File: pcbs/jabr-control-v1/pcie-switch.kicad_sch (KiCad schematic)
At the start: 54 parts, among them U303 PI7C9X2G304SL

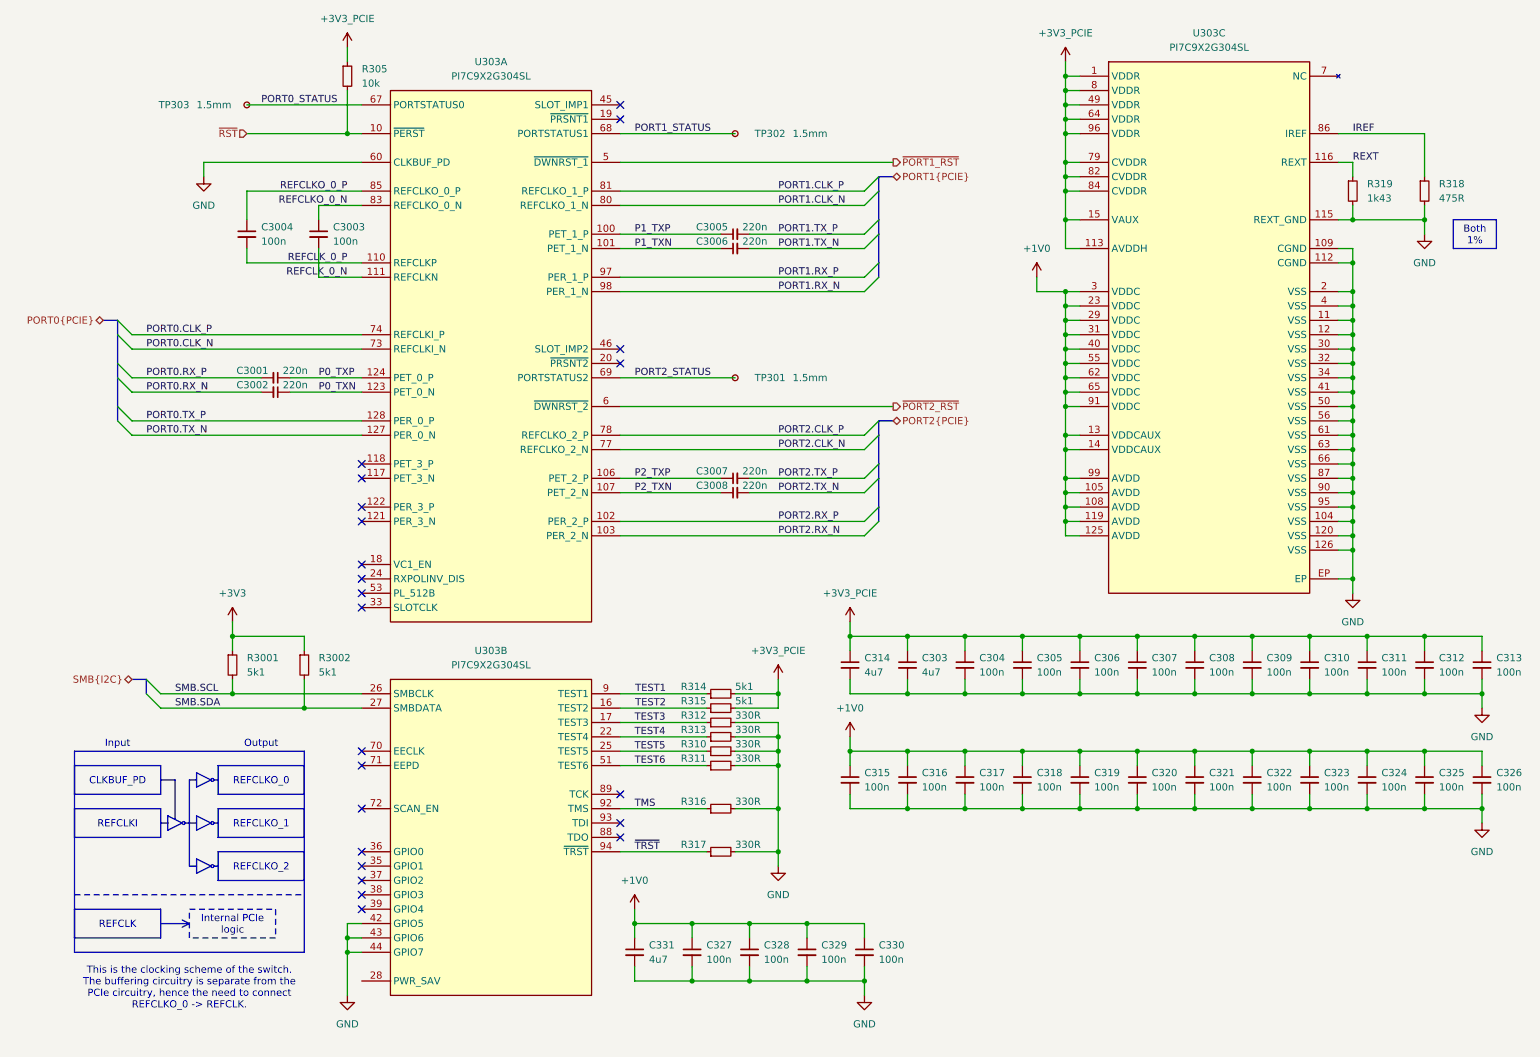
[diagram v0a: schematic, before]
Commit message: Updated FH12-22S-0.5SH footprints
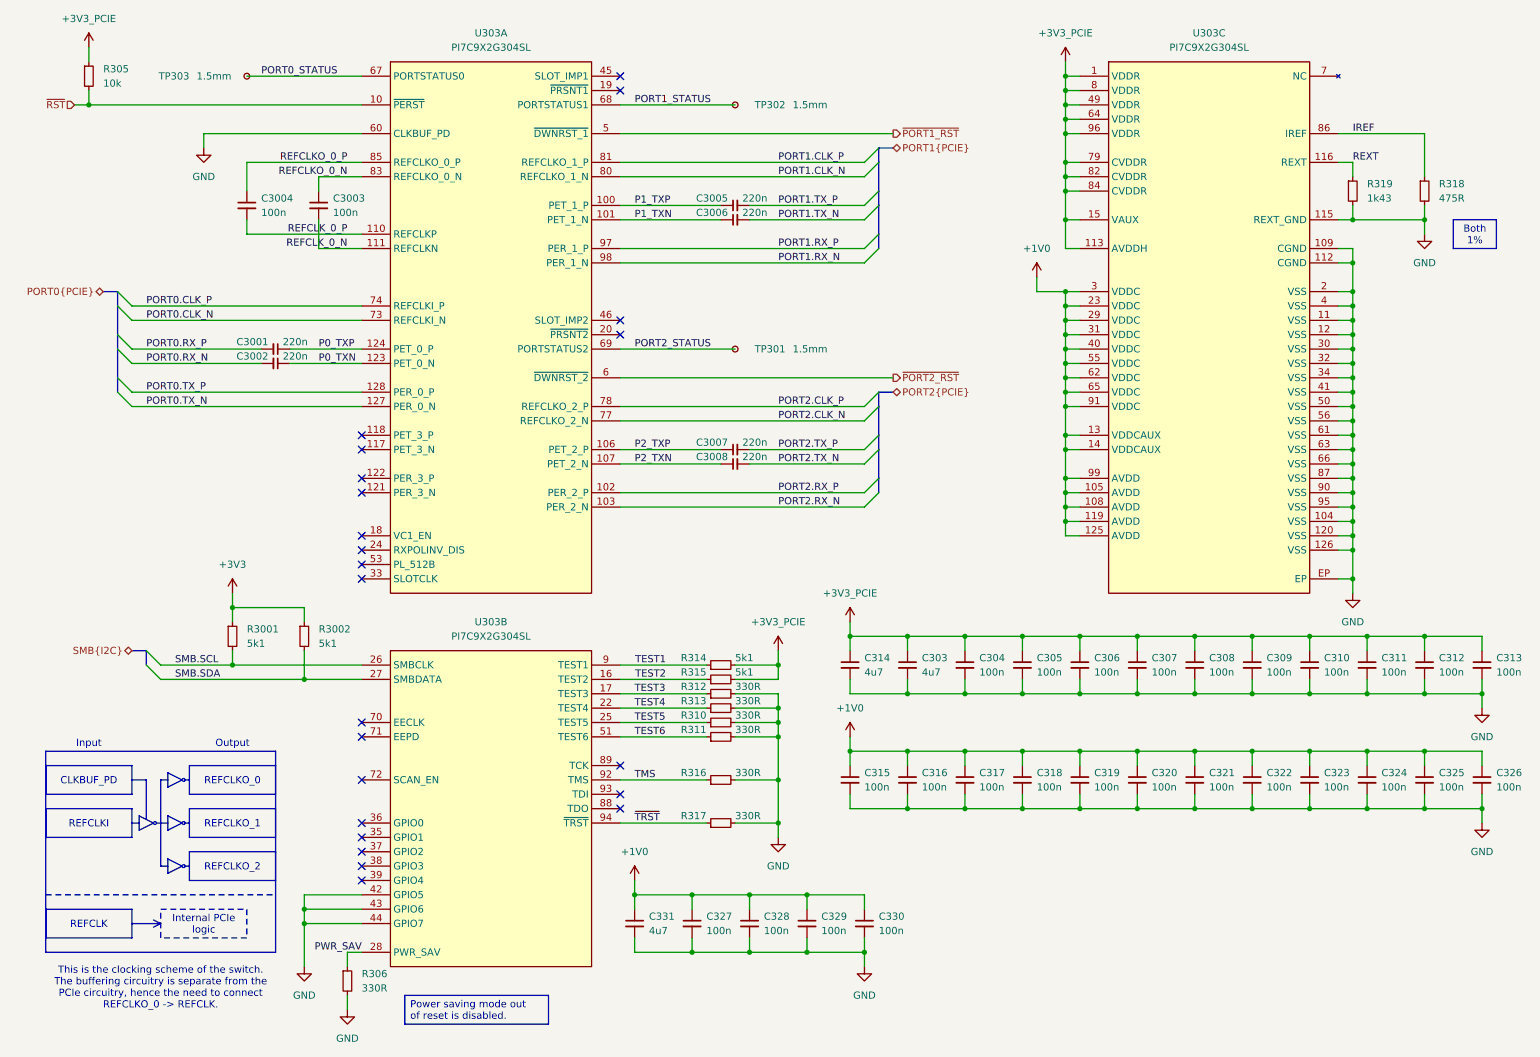
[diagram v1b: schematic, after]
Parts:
- added R306: 330R, project_footprints:R_0402, symbol DEV:R_SMALL
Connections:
- net GND: now also R306.2
- net PWR_SAV: now reaches U303.28 (PWR_SAV)
- net PWR_SAV: now also R306.1
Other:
- moved on the sheet: C3001, C3002, C3003, C3004, C3005, C3006, C3007, C3008, C327, C328, C329, C330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
